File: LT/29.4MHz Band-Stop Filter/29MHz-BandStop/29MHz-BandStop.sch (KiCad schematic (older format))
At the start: 22 parts

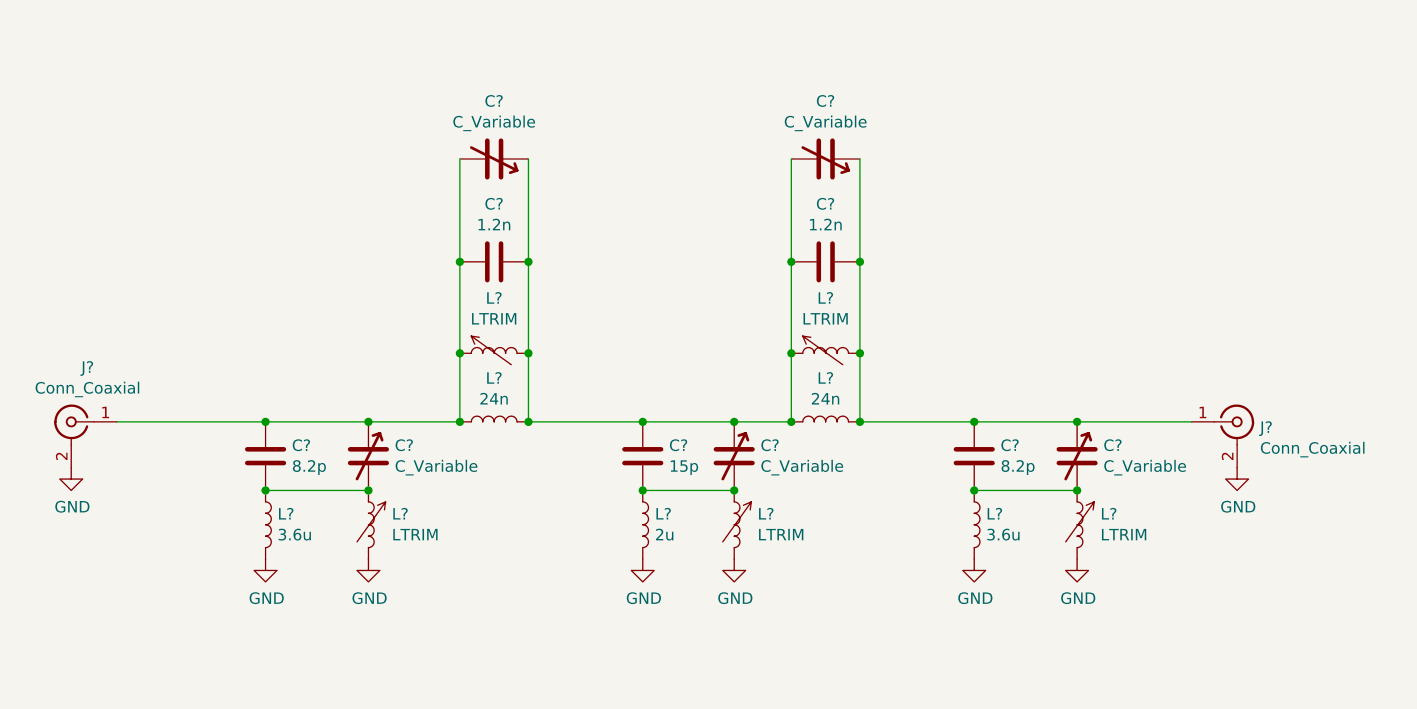
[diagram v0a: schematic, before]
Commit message: created schematic symbol and footprint for 7m3 inductor. laid out PCB
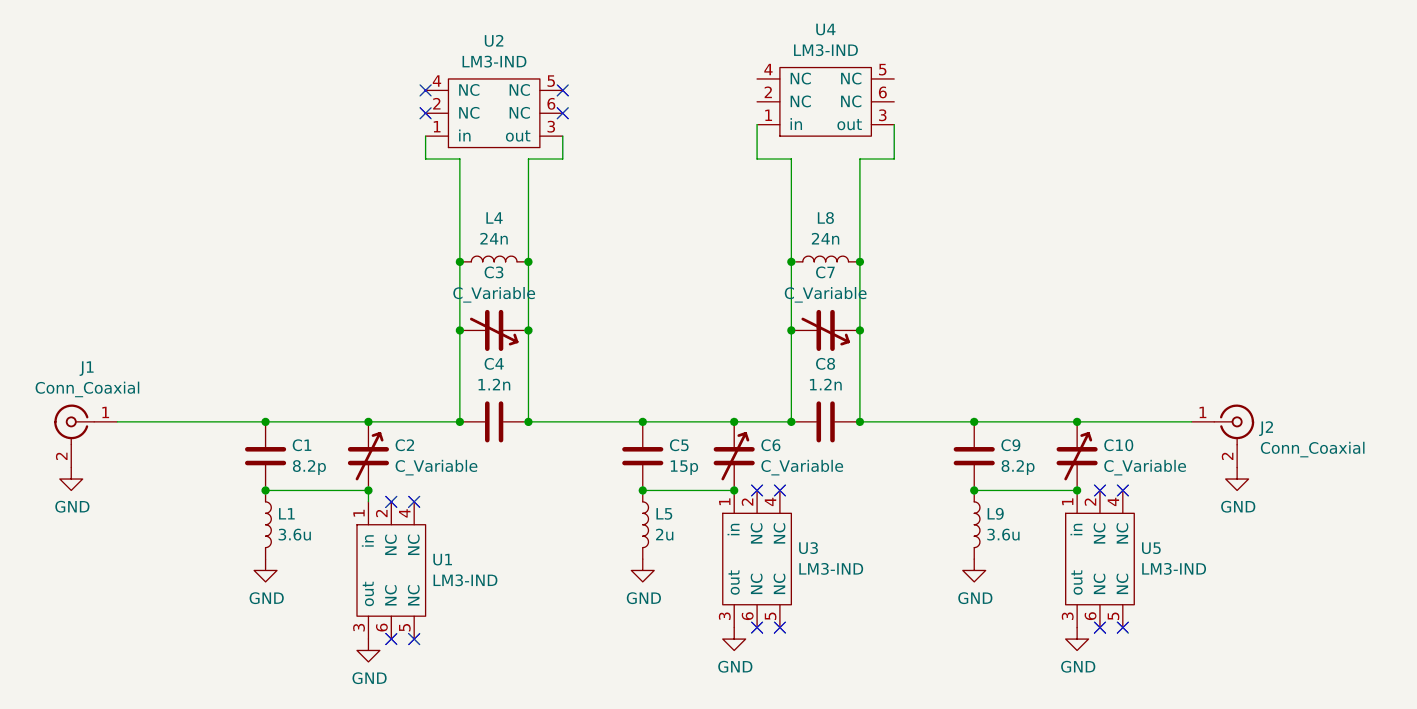
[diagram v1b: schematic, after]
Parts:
- removed L? (x5): LTRIM, symbol Device:LTRIM
- added U1, U2, U3, U4, U5: LM3-IND, LT:IND_trimmer_7M3, symbol LT-Schematics:LM3-IND
- C1, C4, C5, C8, C9: renamed from C?; footprint (none) -> Capacitor_SMD:C_0805_2012Metric_Pad1.15x1.40mm_HandSolder
- C10, C2, C3, C6, C7: renamed from C?; footprint (none) -> LT:CAP_trimmer_SGC3
- J1, J2: renamed from J?; footprint (none) -> Connector_Coaxial:SMA_Molex_73251-1153_EdgeMount_Horizontal
- L1, L4, L5, L8, L9: renamed from L?; footprint (none) -> Capacitor_SMD:C_0805_2012Metric_Pad1.15x1.40mm_HandSolder
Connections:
- net GND: now also U1.3 (out), U3.3 (out), U5.3 (out)
- net at C1.1, C2.1, C3.2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: now also U2.1 (in)
- net at C3.1, C4.2, C5.1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: now also U2.3 (out), U4.1 (in)
- net at C1.2, C2.2, L1.1: now also U1.1 (in)
- net at C10.1, C7.1, C8.2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: now also U4.3 (out)
- net at C5.2, C6.2, L5.1: now also U3.1 (in)
- net at C10.2, C9.2, L9.1: now also U5.1 (in)
- no-connect marks 0 -> 16
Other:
- moved on the sheet: C3, C4, C7, C8, L4, L8
